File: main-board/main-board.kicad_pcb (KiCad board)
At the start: 2 copper layers, 105.4 x 61.6 mm, 18 parts, among them J1 EXP, J2 EXP, SW1 RESET, U1 W65C02S, U2 28C256, U3 AS6C62256, U4 74HC30, U5 74HC00, U6 DS1813, X1 1MHz

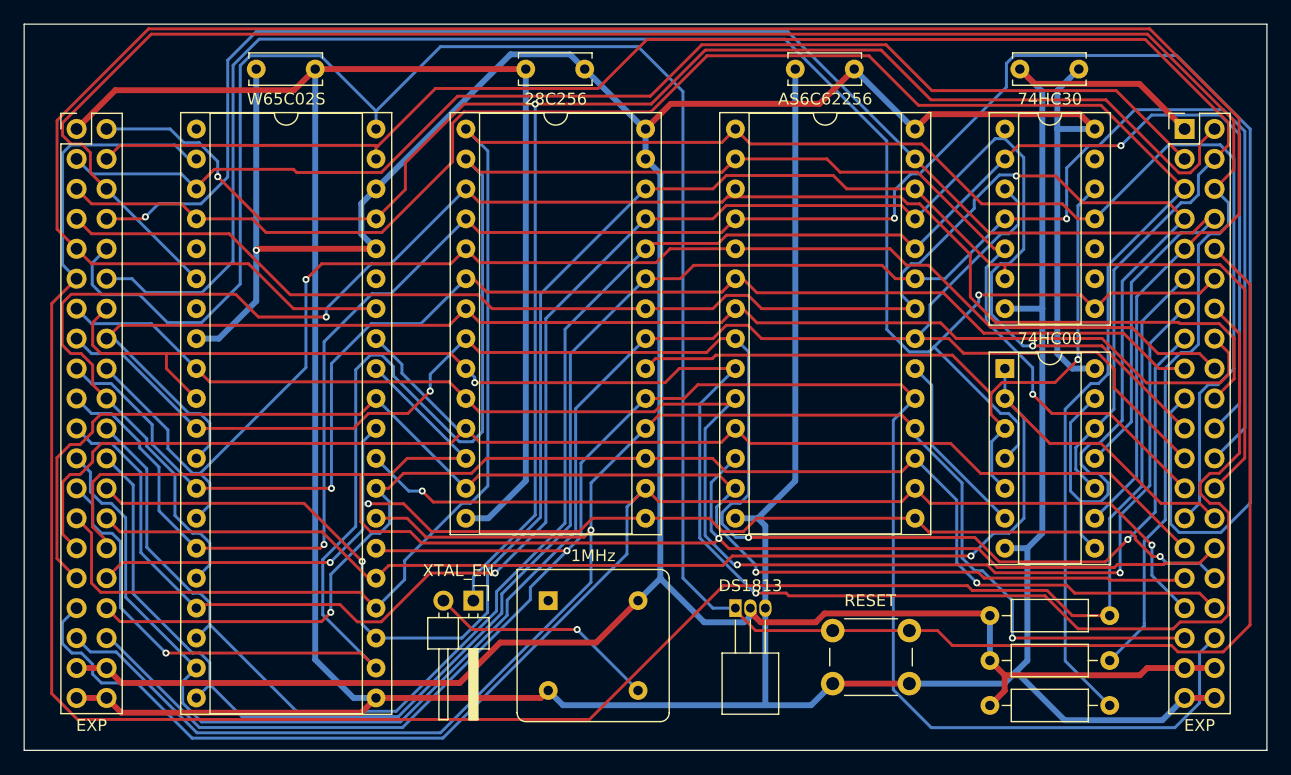
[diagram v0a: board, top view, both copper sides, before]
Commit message: remove old peripheral boards, begn new vga design
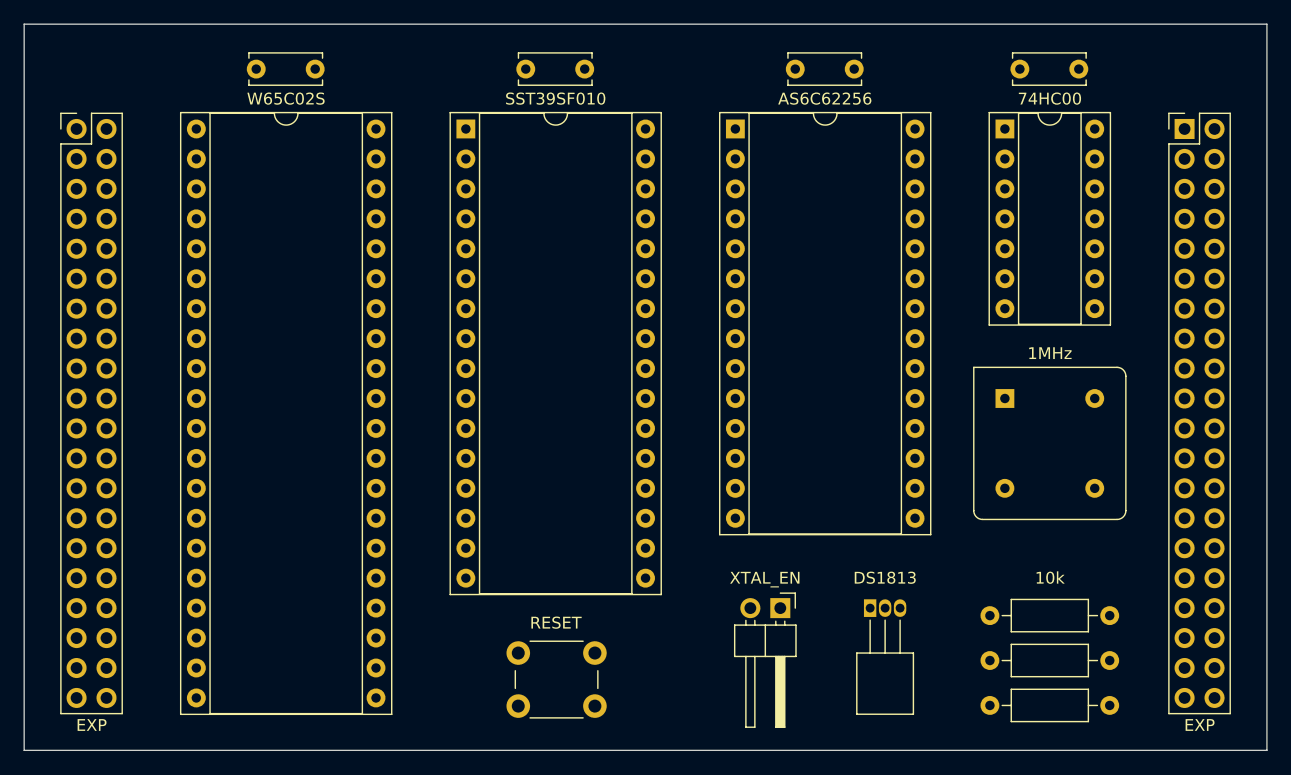
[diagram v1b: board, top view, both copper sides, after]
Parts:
- removed U5: 74HC00, Package_DIP:DIP-14_W7.62mm_Socket
- U2: value 28C256 -> SST39SF010; footprint Package_DIP:DIP-28_W15.24mm_Socket -> Package_DIP:DIP-32_W15.24mm_Socket
- U4: value 74HC30 -> 74HC00
- moved X1 42.4 mm to (149.9, 57.1)
- moved SW1 26.7 mm to (108.6, 78.7)
- moved JP1 26.0 mm to (130.8, 74.9)
- moved U6 11.4 mm to (138.4, 74.9)
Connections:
- J1 pad 1: GND -> PHI1
- J1 pad 10: !RESET -> CLK
- J1 pad 11: RDY -> GND
- J1 pad 12: !P_SELECT -> GND
- J1 pad 2: CLK -> PHI2
- J1 pad 28: A15 -> !RAM_SELECT
- J1 pad 3: PHI1 -> !IRQ
- J1 pad 4: PHI2 -> !NMI
- J1 pad 5: !IRQ -> !READ
- J1 pad 6: !NMI -> !WRITE
- J1 pad 7: !READ -> R!W
- J1 pad 8: !WRITE -> !RESET
- J1 pad 9: R!W -> RDY
- J2 pad 1: GND -> PHI1
- J2 pad 10: !RESET -> CLK
- J2 pad 11: RDY -> GND
- J2 pad 12: !P_SELECT -> GND
- J2 pad 2: CLK -> PHI2
- J2 pad 28: A15 -> !RAM_SELECT
- J2 pad 3: PHI1 -> !IRQ
- J2 pad 4: PHI2 -> !NMI
- J2 pad 5: !IRQ -> !READ
- J2 pad 6: !NMI -> !WRITE
- J2 pad 7: !READ -> R!W
- J2 pad 8: !WRITE -> !RESET
- J2 pad 9: R!W -> RDY
- U1 pad 25: A15 -> !RAM_SELECT
- U2 pad 1: A14 -> Net-(U2-Pad1)
- U2 pad 10: A0 -> A2
- U2 pad 11: D0 -> A1
- U2 pad 12: D1 -> A0
- U2 pad 13: D2 -> D0
- U2 pad 14: GND -> D1
- U2 pad 15: D3 -> D2
- U2 pad 16: D4 -> GND
- U2 pad 17: D5 -> D3
- U2 pad 18: D6 -> D4
- U2 pad 19: D7 -> D5
- U2 pad 2: A12 -> GND
- U2 pad 20: !ROM_SELECT -> D6
- U2 pad 21: A10 -> D7
- U2 pad 22: !READ -> !ROM_SELECT
- U2 pad 23: A11 -> A10
- U2 pad 24: A9 -> !READ
- U2 pad 25: A8 -> A11
- U2 pad 26: A13 -> A9
- U2 pad 27: +5V -> A8
- U2 pad 28: +5V -> A13
- U2 pad 3: A7 -> GND
- U2 pad 4: A6 -> A12
- U2 pad 5: A5 -> A7
- U2 pad 6: A4 -> A6
- U2 pad 7: A3 -> A5
- U2 pad 8: A2 -> A4
- U2 pad 9: A1 -> A3
- U4 pad 1: A8 -> A14
- U4 pad 10: (no net) -> PHI2
- U4 pad 11: A14 -> !WRITE
- U4 pad 12: !ROM_SELECT -> PHI2
- U4 pad 13: (no net) -> !READ
- U4 pad 2: A9 -> !RAM_SELECT
- U4 pad 3: A10 -> !ROM_SELECT
- U4 pad 4: A11 -> (no net)
- U4 pad 5: A12 -> (no net)
- U4 pad 6: A13 -> (no net)
- U4 pad 8: !P_SELECT -> !READ
- U4 pad 9: (no net) -> R!W
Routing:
- net GND: track 371.5 -> 0.00 mm
- net +5V: track 298.3 -> 0.00 mm, vias 1 -> 0
- net !RESET: track 208.7 -> 0.00 mm
- net A6: track 191.7 -> 0.00 mm, vias 2 -> 0
- net RDY: track 186.9 -> 0.00 mm
- net R!W: track 185.7 -> 0.00 mm
- net A12: track 183.8 -> 0.00 mm, vias 2 -> 0
- net A14: track 181.9 -> 0.00 mm
- net A11: track 177.6 -> 0.00 mm, vias 1 -> 0
- net !NMI: track 176.0 -> 0.00 mm
- net A9: track 171.7 -> 0.00 mm, vias 1 -> 0
- net D7: track 164.5 -> 0.00 mm, vias 1 -> 0
- net A1: track 159.9 -> 0.00 mm, vias 2 -> 0
- net !IRQ: track 158.3 -> 0.00 mm
- net A13: track 157.5 -> 0.00 mm, vias 1 -> 0
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
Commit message: reroute main board and IO board again
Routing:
- net GND: track 0.00 -> 385.9 mm
- net +5V: track 0.00 -> 282.2 mm, vias 0 -> 2
- net !IRQ: track 0.00 -> 200.2 mm
- net A14: track 0.00 -> 198.8 mm
- net A8: track 0.00 -> 193.3 mm, vias 0 -> 3
- net A12: track 0.00 -> 186.6 mm, vias 0 -> 3
- net A13: track 0.00 -> 177.9 mm, vias 0 -> 2
- net !RESET: track 0.00 -> 176.6 mm, vias 0 -> 1
- net RDY: track 0.00 -> 176.5 mm
- net CLK: track 0.00 -> 174.6 mm
- net !NMI: track 0.00 -> 168.8 mm
- net A7: track 0.00 -> 153.7 mm, vias 0 -> 2
- net D4: track 0.00 -> 150.8 mm
- net A6: track 0.00 -> 147.2 mm, vias 0 -> 3
- net A4: track 0.00 -> 141.3 mm, vias 0 -> 2
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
